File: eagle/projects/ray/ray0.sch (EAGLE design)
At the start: 8 parts, among them CN1 1X4SMT, CN2 1X4SMT

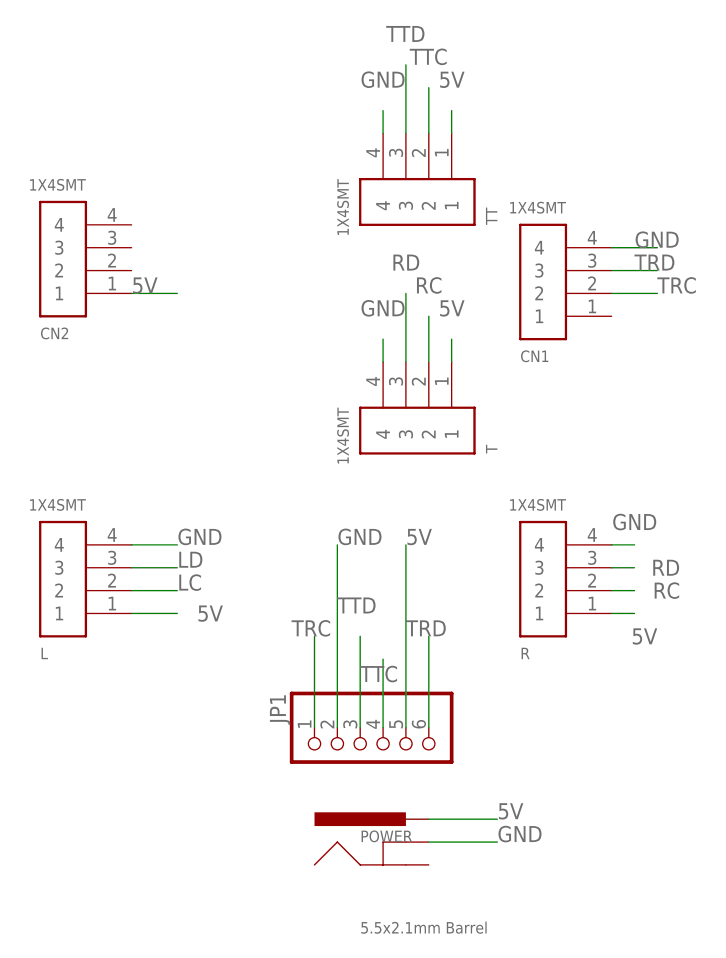
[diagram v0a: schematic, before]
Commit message: make solder pads for LED strips more forgiving
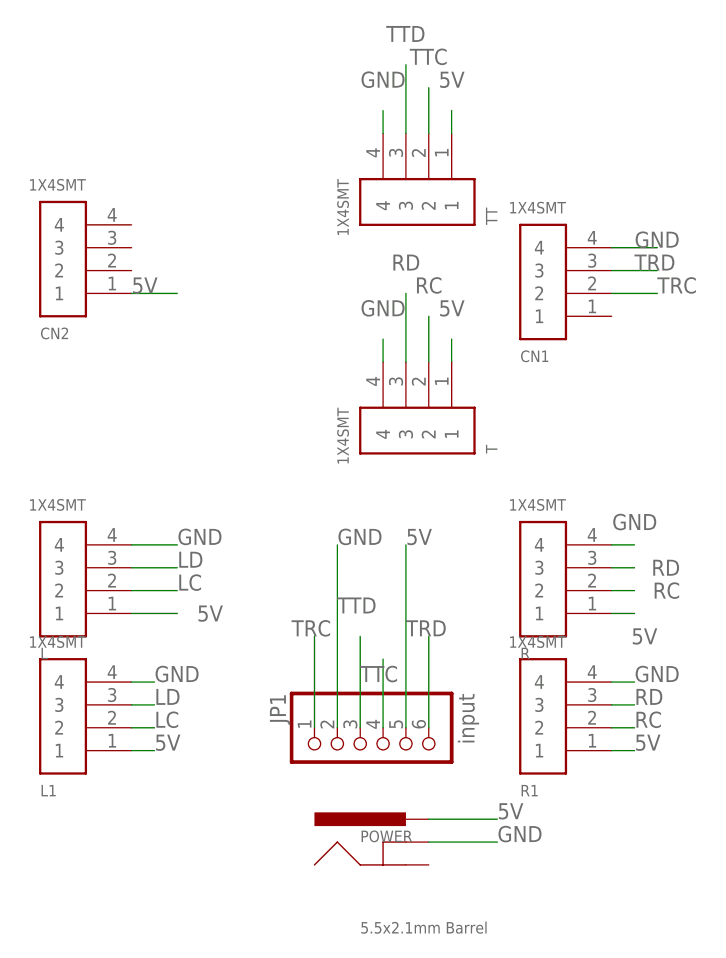
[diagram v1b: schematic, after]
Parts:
- added L1, R1: 1X4SMT, adafruit:1X4SMT
- JP1: value (none) -> input
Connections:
- net 5V: now also L1.1, R1.1
- net GND: now also L1.4, R1.4
- net LC: now also L1.2
- net LD: now also L1.3
- net RC: now also R1.2
- net RD: now also R1.3
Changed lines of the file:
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@@
 <part name="TT" library="adafruit" library_urn="urn:adsk.eagle:library:420" deviceset="1X4" device="SMT" package3d_urn="urn:adsk.eagle:package:6240933/1"/>
 <part name="POWER" library="SparkFun-Connectors" deviceset="POWER_JACK" device="SMD" value="5.5x2.1mm Barrel"/>
-<part name="JP1" library="pinhead" library_urn="urn:adsk.eagle:library:325" deviceset="PINHD-1X6" device="" package3d_urn="urn:adsk.eagle:package:22472/2"/>
+<part name="JP1" library="pinhead" library_urn="urn:adsk.eagle:library:325" deviceset="PINHD-1X6" device="" package3d_urn="urn:adsk.eagle:package:22472/2" value="input"/>
 <part name="CN1" library="adafruit" library_urn="urn:adsk.eagle:library:420" deviceset="1X4" device="SMT" package3d_urn="urn:adsk.eagle:package:6240933/1"/>
 <part name="CN2" library="adafruit" library_urn="urn:adsk.eagle:library:420" deviceset="1X4" device="SMT" package3d_urn="urn:adsk.eagle:package:6240933/1"/>
+<part name="L1" library="adafruit" library_urn="urn:adsk.eagle:library:420" deviceset="1X4" device="SMT" package3d_urn="urn:adsk.eagle:package:6240933/1"/>
+<part name="R1" library="adafruit" library_urn="urn:adsk.eagle:library:420" deviceset="1X4" device="SMT" package3d_urn="urn:adsk.eagle:package:6240933/1"/>
 </parts>
 <sheets>
@@
 <attribute name="VALUE" x="17.78" y="104.14" size="1.27" layer="96" font="vector" rot="R180"/>
 </instance>
+<instance part="L1" gate="G$1" x="17.78" y="43.18" smashed="yes" rot="R180">
+<attribute name="NAME" x="12.7" y="35.56" size="1.27" layer="95" font="vector"/>
+<attribute name="VALUE" x="17.78" y="53.34" size="1.27" layer="96" font="vector" rot="R180"/>
+</instance>
+<instance part="R1" gate="G$1" x="71.12" y="43.18" smashed="yes" rot="R180">
+<attribute name="NAME" x="66.04" y="35.56" size="1.27" layer="95" font="vector"/>
+<attribute name="VALUE" x="71.12" y="53.34" size="1.27" layer="96" font="vector" rot="R180"/>
+</instance>
 </instances>
 <busses>
@@
 <label x="22.86" y="91.44" size="1.778" layer="95"/>
 </segment>
+<segment>
+<pinref part="L1" gate="G$1" pin="1"/>
+<wire x1="22.86" y1="40.64" x2="25.4" y2="40.64" width="0.1524" layer="91"/>
+<label x="25.4" y="40.64" size="1.778" layer="95"/>
+</segment>
+<segment>
+<pinref part="R1" gate="G$1" pin="1"/>
+<wire x1="76.2" y1="40.64" x2="78.74" y2="40.64" width="0.1524" layer="91"/>
+<label x="78.74" y="40.64" size="1.778" layer="95"/>
+</segment>
 </net>
 <net name="GND" class="0">
@@
 <label x="27.94" y="63.5" size="1.778" layer="95"/>
 </segment>
+<segment>
+<pinref part="L1" gate="G$1" pin="4"/>
+<wire x1="22.86" y1="48.26" x2="25.4" y2="48.26" width="0.1524" layer="91"/>
+<label x="25.4" y="48.26" size="1.778" layer="95"/>
+</segment>
+<segment>
+<pinref part="R1" gate="G$1" pin="4"/>
+<wire x1="76.2" y1="48.26" x2="78.74" y2="48.26" width="0.1524" layer="91"/>
+<label x="78.74" y="48.26" size="1.778" layer="95"/>
+</segment>
 </net>
 <net name="TTC" class="0">
@@
 <label x="55.88" y="91.44" size="1.778" layer="95" align="bottom-center"/>
 </segment>
+<segment>
+<pinref part="R1" gate="G$1" pin="2"/>
+<wire x1="76.2" y1="43.18" x2="78.74" y2="43.18" width="0.1524" layer="91"/>
+<label x="78.74" y="43.18" size="1.778" layer="95"/>
+</segment>
 </net>
 <net name="RD" class="0">
@@
 <label x="53.34" y="93.98" size="1.778" layer="95" align="bottom-center"/>
 </segment>
+<segment>
+<pinref part="R1" gate="G$1" pin="3"/>
+<wire x1="76.2" y1="45.72" x2="78.74" y2="45.72" width="0.1524" layer="91"/>
+<label x="78.74" y="45.72" size="1.778" layer="95"/>
+</segment>
 </net>
 <net name="TRC" class="0">
@@
 <label x="27.94" y="58.42" size="1.778" layer="95"/>
 </segment>
+<segment>
+<pinref part="L1" gate="G$1" pin="2"/>
+<wire x1="22.86" y1="43.18" x2="25.4" y2="43.18" width="0.1524" layer="91"/>
+<label x="25.4" y="43.18" size="1.778" layer="95"/>
+</segment>
 </net>
 <net name="LD" class="0">
@@
 <label x="27.94" y="60.96" size="1.778" layer="95"/>
 </segment>
-</net>
+<segment>
+<pinref part="L1" gate="G$1" pin="3"/>
+<wire x1="22.86" y1="45.72" x2="25.4" y2="45.72" width="0.1524" layer="91"/>
+<label x="25.4" y="45.72" size="1.778" layer="95"/>
+</segment>
+</net>
